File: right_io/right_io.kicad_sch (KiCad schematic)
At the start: 0 parts

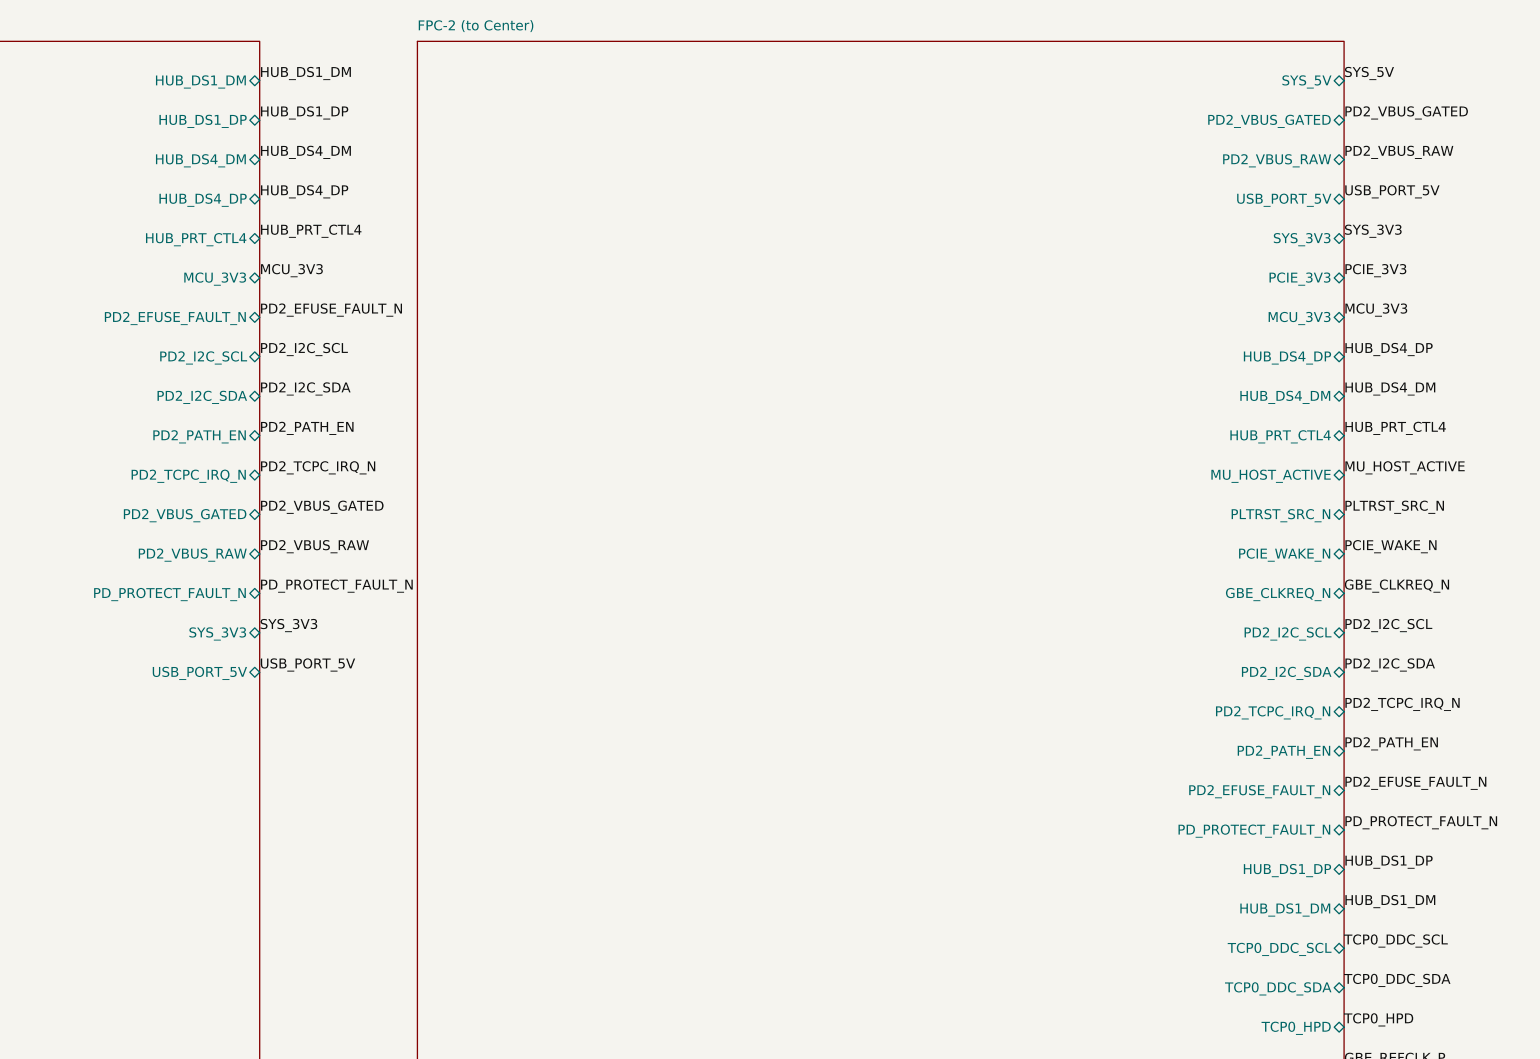
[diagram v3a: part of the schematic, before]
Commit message: get the main boards ready for routing
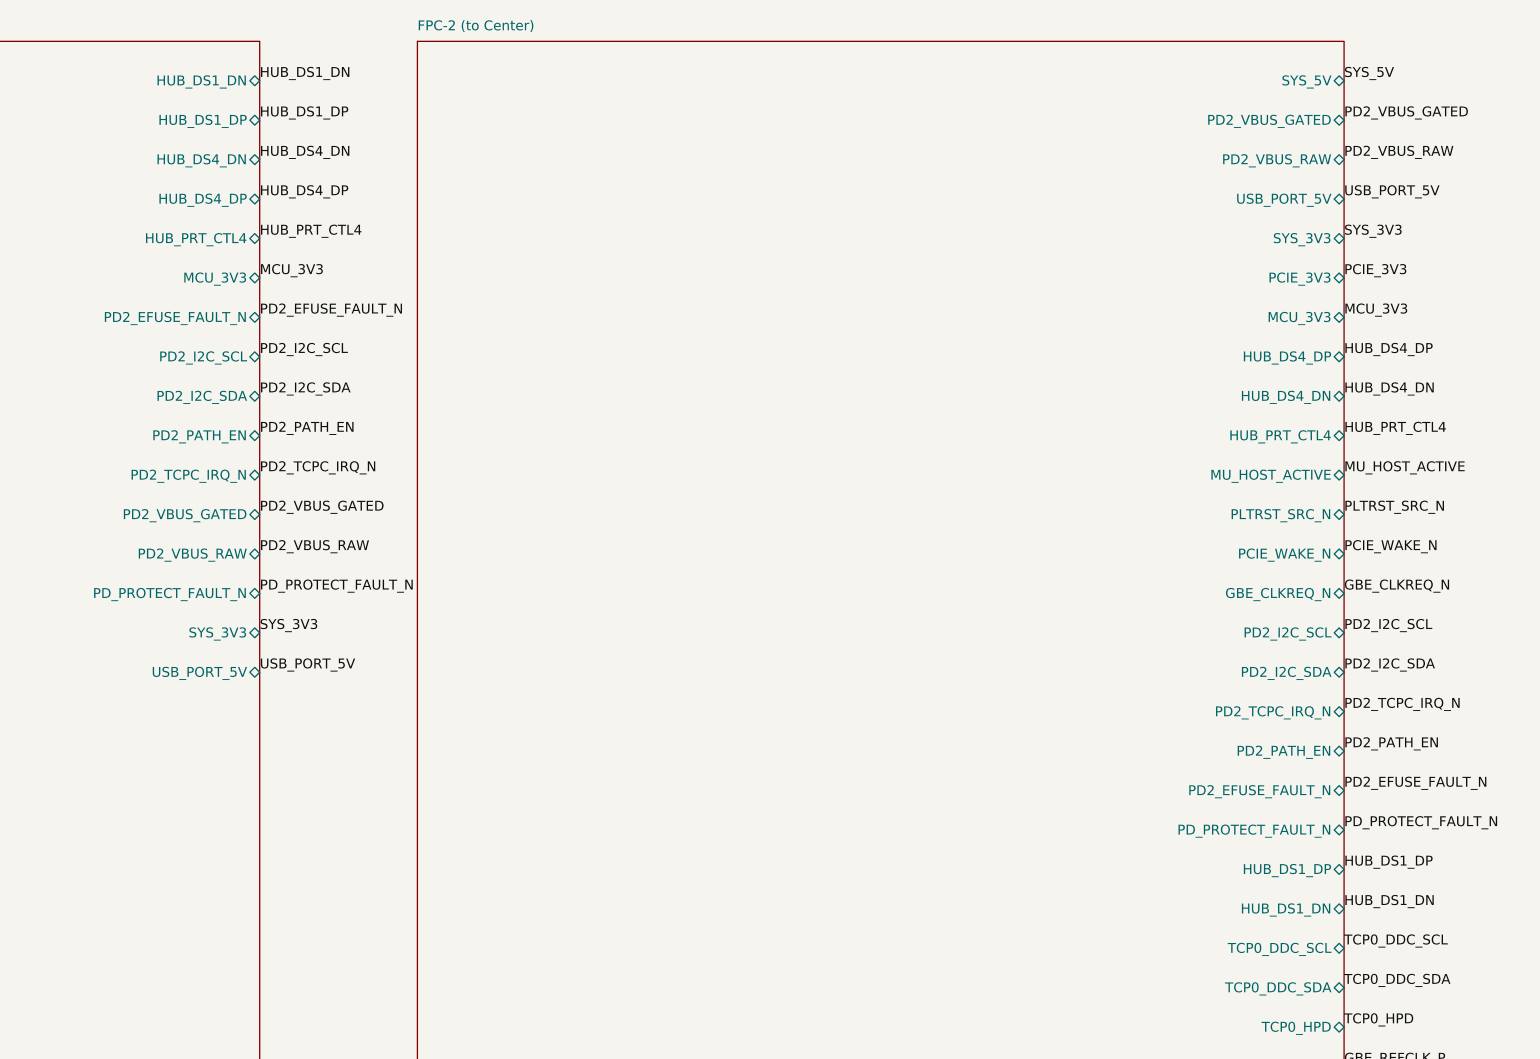
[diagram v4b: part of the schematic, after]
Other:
- sheet FPC-2 (to Center) ports: added HUB_DS1_DN, HUB_DS4_DN; removed HUB_DS1_DM, HUB_DS4_DM
- sheet PD2 Dual-Role ports: added HUB_DS1_DN, HUB_DS4_DN; removed HUB_DS1_DM, HUB_DS4_DM
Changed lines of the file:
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@@
     (effects (font (size 1.27 1.27)) (justify left top))
   )
-  (pin "HUB_DS1_DM" bidirectional
+  (pin "HUB_DS1_DN" bidirectional
     (at 149.86 44.45 0)
     (effects (font (size 1.27 1.27)) (justify left))
@@
     (effects (font (size 1.27 1.27)) (justify left))
   )
-  (pin "HUB_DS4_DM" bidirectional
+  (pin "HUB_DS4_DN" bidirectional
     (at 149.86 54.61 0)
     (effects (font (size 1.27 1.27)) (justify left))
@@
     (effects (font (size 1.27 1.27)) (justify left))
   )
-  (pin "HUB_DS4_DM" bidirectional
+  (pin "HUB_DS4_DN" bidirectional
     (at 289.56 85.09 0)
     (effects (font (size 1.27 1.27)) (justify left))
@@
     (effects (font (size 1.27 1.27)) (justify left))
   )
-  (pin "HUB_DS1_DM" bidirectional
+  (pin "HUB_DS1_DN" bidirectional
     (at 289.56 151.13 0)
     (effects (font (size 1.27 1.27)) (justify left))
@@
   )
 )
-(label "HUB_DS1_DM"
+(label "HUB_DS1_DN"
   (at 149.86 44.45 0)
   (effects (font (size 1.27 1.27)) (justify left bottom))
@@
   (effects (font (size 1.27 1.27)) (justify left bottom))
 )
-(label "HUB_DS4_DM"
+(label "HUB_DS4_DN"
   (at 149.86 54.61 0)
   (effects (font (size 1.27 1.27)) (justify left bottom))
@@
   (effects (font (size 1.27 1.27)) (justify left bottom))
 )
-(label "HUB_DS4_DM"
+(label "HUB_DS4_DN"
   (at 289.56 85.09 0)
   (effects (font (size 1.27 1.27)) (justify left bottom))
@@
   (effects (font (size 1.27 1.27)) (justify left bottom))
 )
-(label "HUB_DS1_DM"
+(label "HUB_DS1_DN"
   (at 289.56 151.13 0)
   (effects (font (size 1.27 1.27)) (justify left bottom))

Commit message: fix the center layout and more board issues
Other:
- sheet FPC-2 (to Center) ports: added PD2_SOURCE_PG, USB_J11_PERMIT, USB_J12_PERMIT; removed none
- sheet PD2 Dual-Role ports: added PD2_SOURCE_PG, USB_J11_PERMIT, USB_J12_PERMIT; removed none

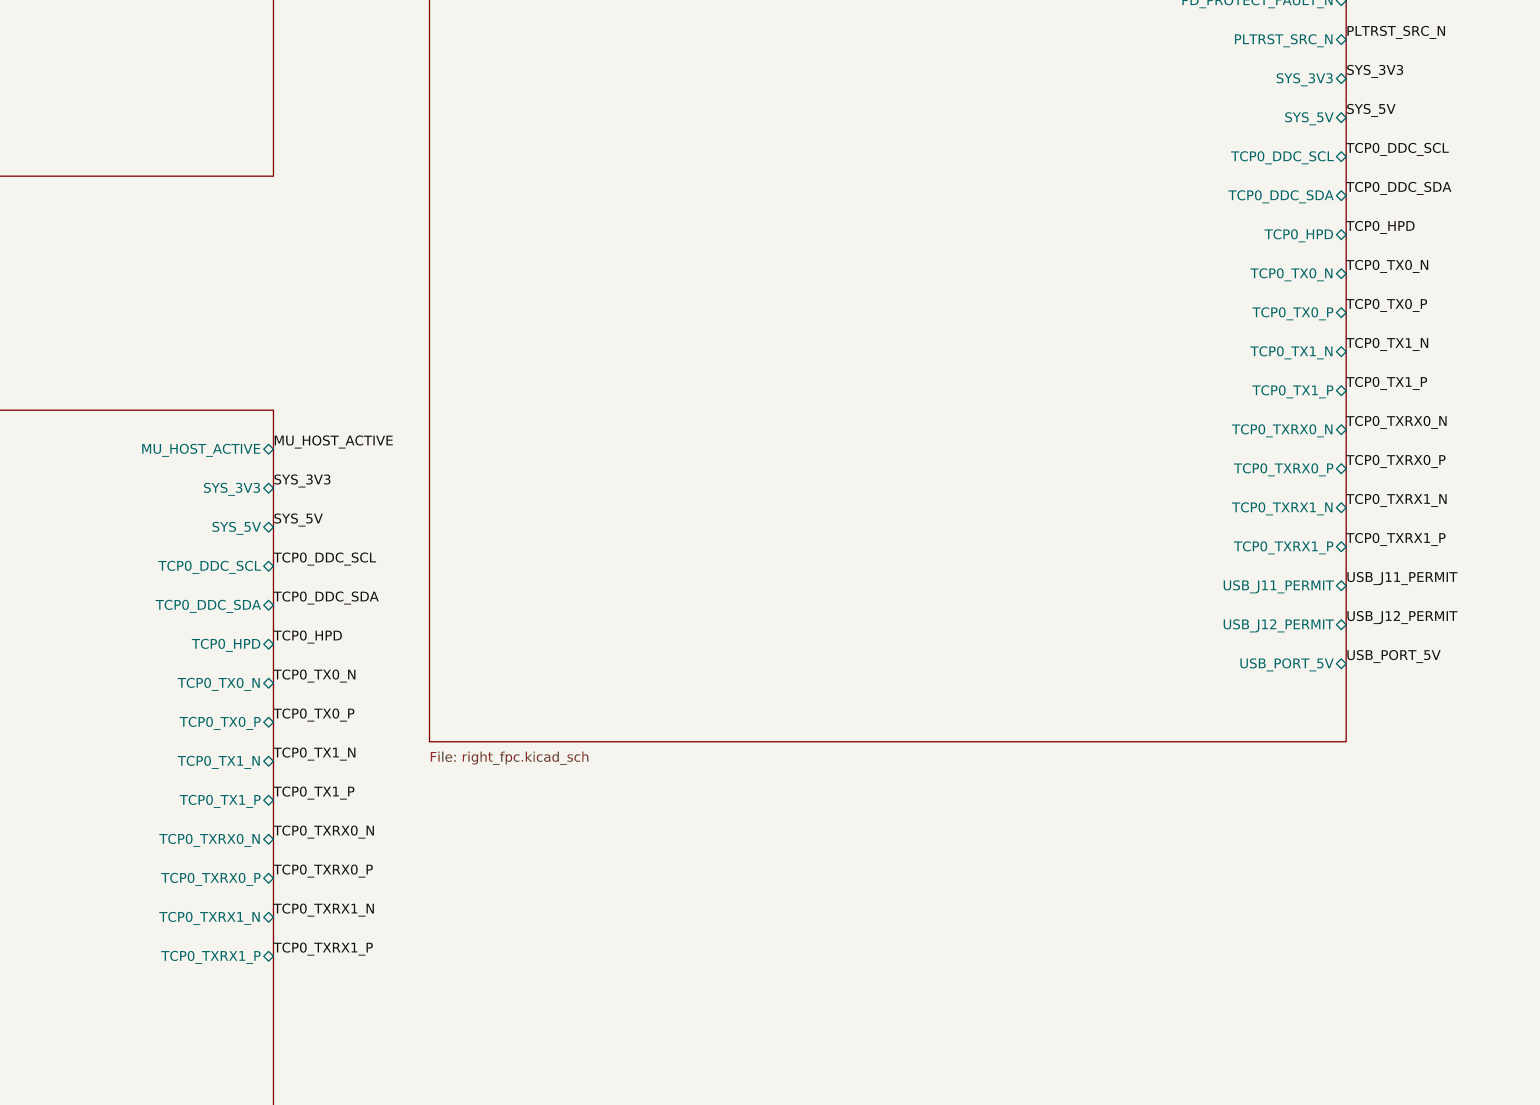
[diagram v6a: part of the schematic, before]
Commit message: start switching the carrier to mu ultra
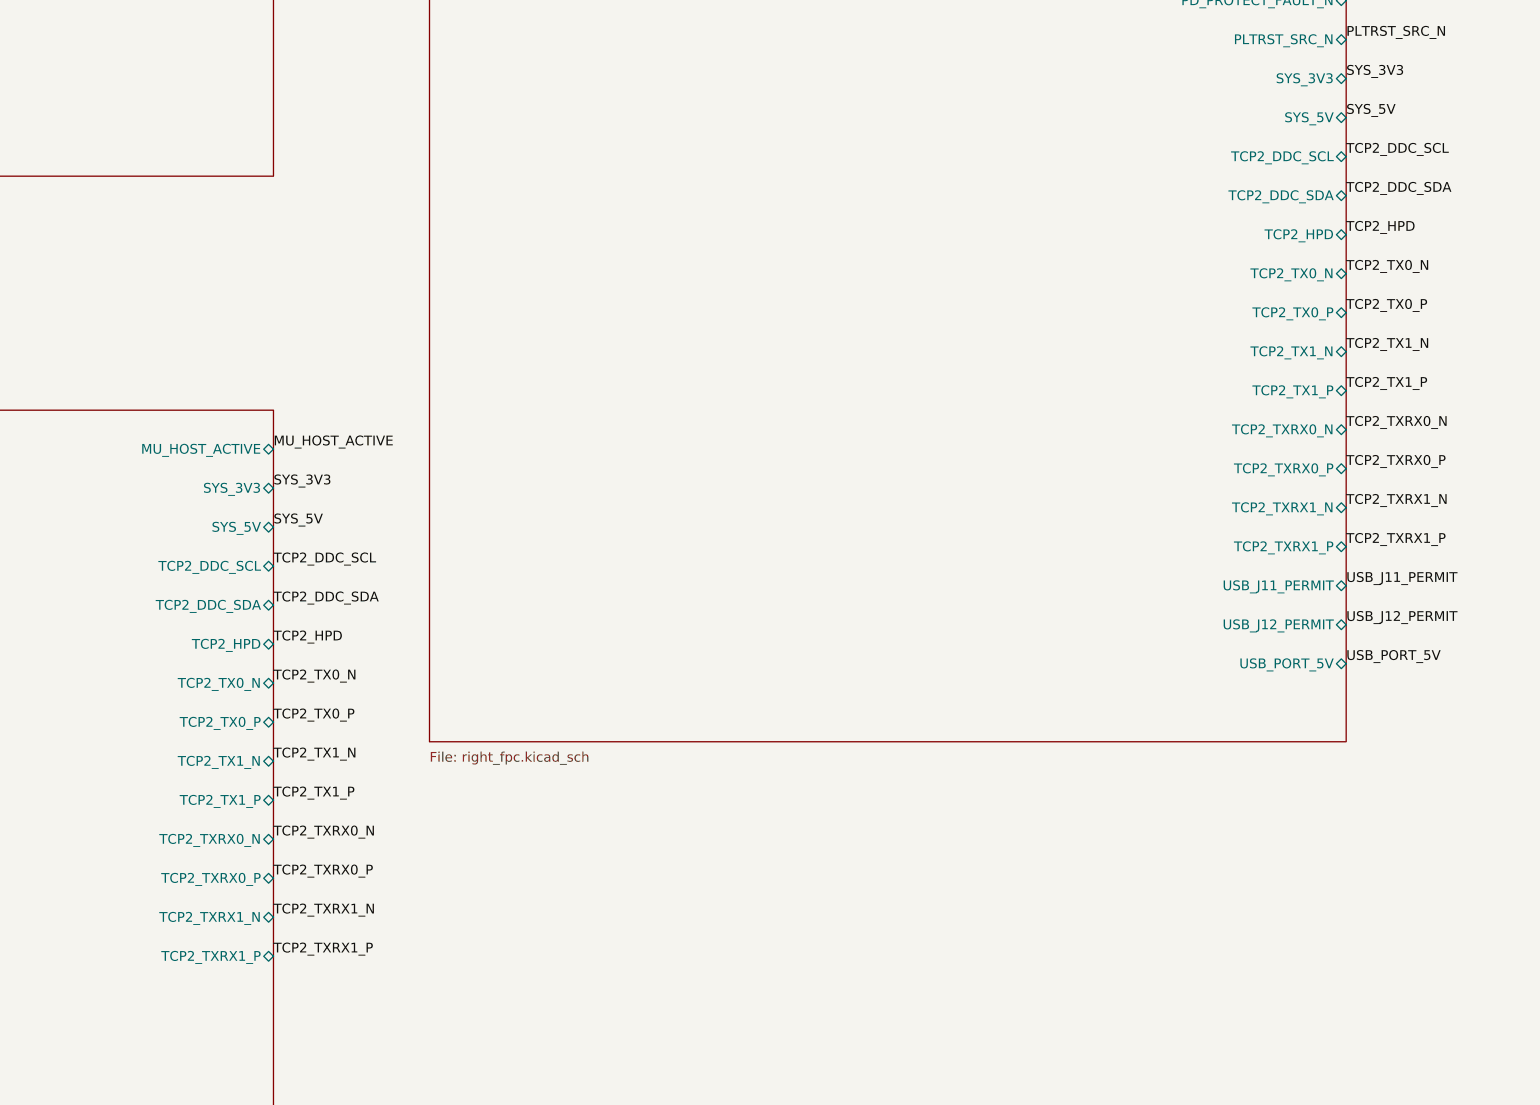
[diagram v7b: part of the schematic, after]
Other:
- sheet FPC-2 (to Center) ports: added TCP2_DDC_SCL, TCP2_DDC_SDA, TCP2_HPD, TCP2_TX0_N, TCP2_TX0_P, TCP2_TX1_N, TCP2_TX1_P, TCP2_TXRX0_N, TCP2_TXRX0_P, TCP2_TXRX1_N, TCP2_TXRX1_P; removed TCP0_DDC_SCL, TCP0_DDC_SDA, TCP0_HPD, TCP0_TX0_N, TCP0_TX0_P, TCP0_TX1_N, TCP0_TX1_P, TCP0_TXRX0_N, TCP0_TXRX0_P, TCP0_TXRX1_N, TCP0_TXRX1_P
- sheet HDMI ports: added TCP2_DDC_SCL, TCP2_DDC_SDA, TCP2_HPD, TCP2_TX0_N, TCP2_TX0_P, TCP2_TX1_N, TCP2_TX1_P, TCP2_TXRX0_N, TCP2_TXRX0_P, TCP2_TXRX1_N, TCP2_TXRX1_P; removed TCP0_DDC_SCL, TCP0_DDC_SDA, TCP0_HPD, TCP0_TX0_N, TCP0_TX0_P, TCP0_TX1_N, TCP0_TX1_P, TCP0_TXRX0_N, TCP0_TXRX0_P, TCP0_TXRX1_N, TCP0_TXRX1_P
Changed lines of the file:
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@@
     (effects (font (size 1.27 1.27)) (justify left))
   )
-  (pin "TCP0_DDC_SCL" bidirectional
+  (pin "TCP2_DDC_SCL" bidirectional
     (at 149.86 240.03 0)
     (effects (font (size 1.27 1.27)) (justify left))
   )
-  (pin "TCP0_DDC_SDA" bidirectional
+  (pin "TCP2_DDC_SDA" bidirectional
     (at 149.86 245.11 0)
     (effects (font (size 1.27 1.27)) (justify left))
   )
-  (pin "TCP0_HPD" bidirectional
+  (pin "TCP2_HPD" bidirectional
     (at 149.86 250.19 0)
     (effects (font (size 1.27 1.27)) (justify left))
   )
-  (pin "TCP0_TX0_N" bidirectional
+  (pin "TCP2_TX0_N" bidirectional
     (at 149.86 255.27 0)
     (effects (font (size 1.27 1.27)) (justify left))
   )
-  (pin "TCP0_TX0_P" bidirectional
+  (pin "TCP2_TX0_P" bidirectional
     (at 149.86 260.35 0)
     (effects (font (size 1.27 1.27)) (justify left))
   )
-  (pin "TCP0_TX1_N" bidirectional
+  (pin "TCP2_TX1_N" bidirectional
     (at 149.86 265.43 0)
     (effects (font (size 1.27 1.27)) (justify left))
   )
-  (pin "TCP0_TX1_P" bidirectional
+  (pin "TCP2_TX1_P" bidirectional
     (at 149.86 270.51 0)
     (effects (font (size 1.27 1.27)) (justify left))
   )
-  (pin "TCP0_TXRX0_N" bidirectional
+  (pin "TCP2_TXRX0_N" bidirectional
     (at 149.86 275.59 0)
     (effects (font (size 1.27 1.27)) (justify left))
   )
-  (pin "TCP0_TXRX0_P" bidirectional
+  (pin "TCP2_TXRX0_P" bidirectional
     (at 149.86 280.67 0)
     (effects (font (size 1.27 1.27)) (justify left))
   )
-  (pin "TCP0_TXRX1_N" bidirectional
+  (pin "TCP2_TXRX1_N" bidirectional
     (at 149.86 285.75 0)
     (effects (font (size 1.27 1.27)) (justify left))
   )
-  (pin "TCP0_TXRX1_P" bidirectional
+  (pin "TCP2_TXRX1_P" bidirectional
     (at 149.86 290.83 0)
     (effects (font (size 1.27 1.27)) (justify left))
@@
     (effects (font (size 1.27 1.27)) (justify left))
   )
-  (pin "TCP0_DDC_SCL" bidirectional
+  (pin "TCP2_DDC_SCL" bidirectional
     (at 289.56 186.69 0)
     (effects (font (size 1.27 1.27)) (justify left))
   )
-  (pin "TCP0_DDC_SDA" bidirectional
+  (pin "TCP2_DDC_SDA" bidirectional
     (at 289.56 191.77 0)
     (effects (font (size 1.27 1.27)) (justify left))
   )
-  (pin "TCP0_HPD" bidirectional
+  (pin "TCP2_HPD" bidirectional
     (at 289.56 196.85 0)
     (effects (font (size 1.27 1.27)) (justify left))
   )
-  (pin "TCP0_TX0_N" bidirectional
+  (pin "TCP2_TX0_N" bidirectional
     (at 289.56 201.93 0)
     (effects (font (size 1.27 1.27)) (justify left))
   )
-  (pin "TCP0_TX0_P" bidirectional
+  (pin "TCP2_TX0_P" bidirectional
     (at 289.56 207.01 0)
     (effects (font (size 1.27 1.27)) (justify left))
   )
-  (pin "TCP0_TX1_N" bidirectional
+  (pin "TCP2_TX1_N" bidirectional
     (at 289.56 212.09 0)
     (effects (font (size 1.27 1.27)) (justify left))
   )
-  (pin "TCP0_TX1_P" bidirectional
+  (pin "TCP2_TX1_P" bidirectional
     (at 289.56 217.17 0)
     (effects (font (size 1.27 1.27)) (justify left))
   )
-  (pin "TCP0_TXRX0_N" bidirectional
+  (pin "TCP2_TXRX0_N" bidirectional
     (at 289.56 222.25 0)
     (effects (font (size 1.27 1.27)) (justify left))
   )
-  (pin "TCP0_TXRX0_P" bidirectional
+  (pin "TCP2_TXRX0_P" bidirectional
     (at 289.56 227.33 0)
     (effects (font (size 1.27 1.27)) (justify left))
   )
-  (pin "TCP0_TXRX1_N" bidirectional
+  (pin "TCP2_TXRX1_N" bidirectional
     (at 289.56 232.41 0)
     (effects (font (size 1.27 1.27)) (justify left))
   )
-  (pin "TCP0_TXRX1_P" bidirectional
+  (pin "TCP2_TXRX1_P" bidirectional
     (at 289.56 237.49 0)
     (effects (font (size 1.27 1.27)) (justify left))
@@
   (effects (font (size 1.27 1.27)) (justify left bottom))
 )
-(label "TCP0_DDC_SCL"
+(label "TCP2_DDC_SCL"
   (at 149.86 240.03 0)
   (effects (font (size 1.27 1.27)) (justify left bottom))
 )
-(label "TCP0_DDC_SDA"
+(label "TCP2_DDC_SDA"
   (at 149.86 245.11 0)
   (effects (font (size 1.27 1.27)) (justify left bottom))
 )
-(label "TCP0_HPD"
+(label "TCP2_HPD"
   (at 149.86 250.19 0)
   (effects (font (size 1.27 1.27)) (justify left bottom))
 )
-(label "TCP0_TX0_N"
+(label "TCP2_TX0_N"
   (at 149.86 255.27 0)
   (effects (font (size 1.27 1.27)) (justify left bottom))
 )
-(label "TCP0_TX0_P"
+(label "TCP2_TX0_P"
   (at 149.86 260.35 0)
   (effects (font (size 1.27 1.27)) (justify left bottom))
 )
-(label "TCP0_TX1_N"
+(label "TCP2_TX1_N"
   (at 149.86 265.43 0)
   (effects (font (size 1.27 1.27)) (justify left bottom))
 )
-(label "TCP0_TX1_P"
+(label "TCP2_TX1_P"
   (at 149.86 270.51 0)
   (effects (font (size 1.27 1.27)) (justify left bottom))
 )
-(label "TCP0_TXRX0_N"
+(label "TCP2_TXRX0_N"
   (at 149.86 275.59 0)
   (effects (font (size 1.27 1.27)) (justify left bottom))
 )
-(label "TCP0_TXRX0_P"
+(label "TCP2_TXRX0_P"
   (at 149.86 280.67 0)
   (effects (font (size 1.27 1.27)) (justify left bottom))
 )
-(label "TCP0_TXRX1_N"
+(label "TCP2_TXRX1_N"
   (at 149.86 285.75 0)
   (effects (font (size 1.27 1.27)) (justify left bottom))
 )
-(label "TCP0_TXRX1_P"
+(label "TCP2_TXRX1_P"
   (at 149.86 290.83 0)
   (effects (font (size 1.27 1.27)) (justify left bottom))
@@
   (effects (font (size 1.27 1.27)) (justify left bottom))
 )
-(label "TCP0_DDC_SCL"
+(label "TCP2_DDC_SCL"
   (at 289.56 186.69 0)
   (effects (font (size 1.27 1.27)) (justify left bottom))
 )
-(label "TCP0_DDC_SDA"
+(label "TCP2_DDC_SDA"
   (at 289.56 191.77 0)
   (effects (font (size 1.27 1.27)) (justify left bottom))
 )
-(label "TCP0_HPD"
+(label "TCP2_HPD"
   (at 289.56 196.85 0)
   (effects (font (size 1.27 1.27)) (justify left bottom))
 )
-(label "TCP0_TX0_N"
+(label "TCP2_TX0_N"
   (at 289.56 201.93 0)
   (effects (font (size 1.27 1.27)) (justify left bottom))
 )
-(label "TCP0_TX0_P"
+(label "TCP2_TX0_P"
   (at 289.56 207.01 0)
   (effects (font (size 1.27 1.27)) (justify left bottom))
 )
-(label "TCP0_TX1_N"
+(label "TCP2_TX1_N"
   (at 289.56 212.09 0)
   (effects (font (size 1.27 1.27)) (justify left bottom))
 )
-(label "TCP0_TX1_P"
+(label "TCP2_TX1_P"
   (at 289.56 217.17 0)
   (effects (font (size 1.27 1.27)) (justify left bottom))
 )
-(label "TCP0_TXRX0_N"
+(label "TCP2_TXRX0_N"
   (at 289.56 222.25 0)
   (effects (font (size 1.27 1.27)) (justify left bottom))
 )
-(label "TCP0_TXRX0_P"
+(label "TCP2_TXRX0_P"
   (at 289.56 227.33 0)
   (effects (font (size 1.27 1.27)) (justify left bottom))
 )
-(label "TCP0_TXRX1_N"
+(label "TCP2_TXRX1_N"
   (at 289.56 232.41 0)
   (effects (font (size 1.27 1.27)) (justify left bottom))
 )
-(label "TCP0_TXRX1_P"
+(label "TCP2_TXRX1_P"
   (at 289.56 237.49 0)
   (effects (font (size 1.27 1.27)) (justify left bottom))
